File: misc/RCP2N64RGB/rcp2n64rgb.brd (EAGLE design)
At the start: 149.4 x 21.1 mm, 67 parts

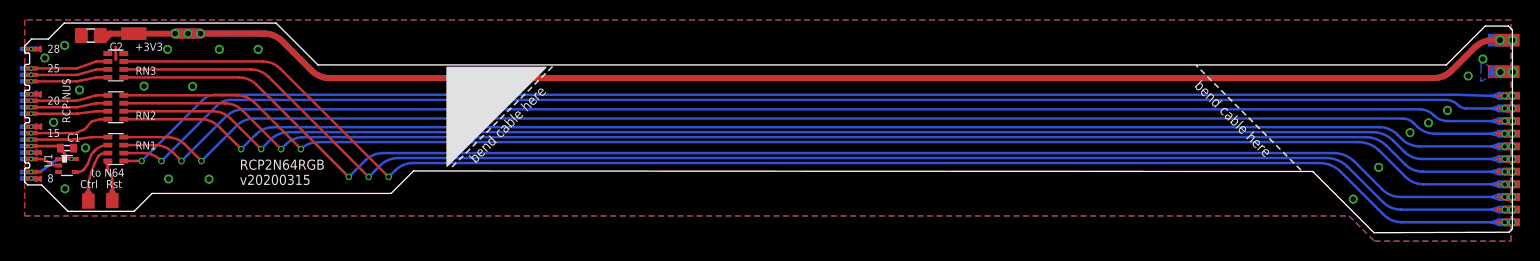
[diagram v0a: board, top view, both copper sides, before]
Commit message: update flex PCBs with suitable buffering
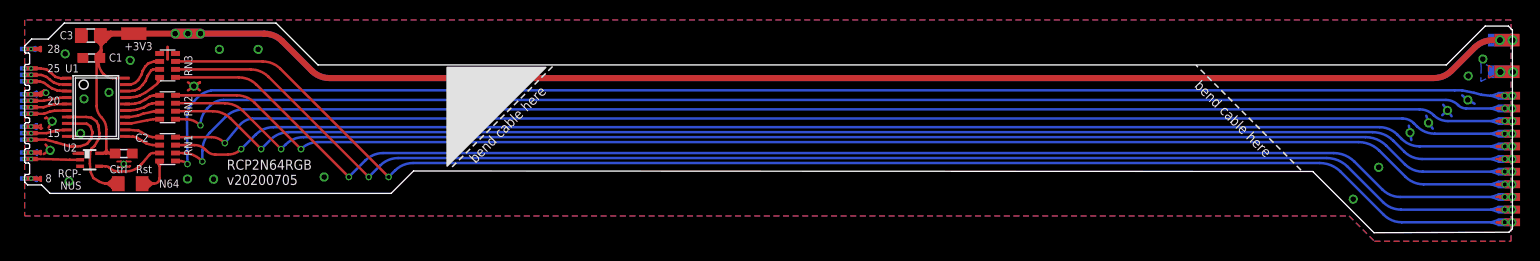
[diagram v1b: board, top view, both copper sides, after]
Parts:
- removed E$1, E$3, E$4, E$5: (no value), wirepad:SMD0,45-1,35
- added C3: 22u, rcl:C0805
- added U2: SN74LVC1G17DCKR, texas:DCK_R-PDSO-G5
- C1: value (none) -> 0.1u; device rcl:C0402 -> rcl:C0603
- C2: value 22u -> 0.1u; device rcl:C0805 -> rcl:C0603
- U1: value (none) -> 74VHC9151FT; device 74xx-little-de:DCK_R-PDSO-G5 -> sipex:TSSOP20
- moved C2 12.3 mm to (9.95, 0.55), turned to 0 degrees
- moved C1 9.38 mm to (6.70, 10.2), turned to 180 degrees
- moved U1 6.53 mm to (7.15, 5.20)
- moved RN1 5.20 mm to (14.3, 1.00)
- moved RN2 5.20 mm to (14.3, 5.20)
- moved RN3 5.20 mm to (14.3, 9.40)
- moved E$2 3.47 mm to (9.40, -2.48)
- moved E$6 3.45 mm to (11.8, -2.48)
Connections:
- removed net VCC: C1.1, E$1.P$1, E$3.P$1, E$4.P$1, E$5.P$1, U1.5
- removed net VCLK_BUF: RN1.2, U1.4
- new net S$1: RN3.2, U1.19
- new net S$10: RN2.4, U1.13
- new net S$11: RN1.3, U2.4
- new net S$12: RN1.2, U1.11
- new net S$2: RN3.3, U1.18
- new net S$3: RN3.4, U1.17
- new net S$4: RN2.1, U1.16
- new net S$6: RN2.2, U1.15
- new net S$7: RN2.3, U1.14
- new net S$9: RN1.1, U1.12
- net #DSYNC: now also U1.8; no longer RN1.1
- net 3V3: now also C1.1, C3.1, U1.20, U2.5
- net CTRL: now also U1.7; no longer RN1.3
- net CTRL.1: now also RN2.5; no longer RN1.6
- net D0: now also U1.1; no longer RN3.2
- net D1: now also U1.2; no longer RN3.3
- net D2: now also U1.3; no longer RN3.4
- net D3: now also U1.4; no longer RN2.1
- net D4: now also U1.5; no longer RN2.2
- net D5: now also U1.6; no longer RN2.3
- net D6: now also U1.9; no longer RN2.4
- net D6.1: now also RN1.7; no longer RN2.5
- net GND: now also C3.2, U1.10, U2.3; no longer U1.3
- net VCLK: now also U2.2; no longer U1.2
- net VCLK.1: now also RN1.6; no longer RN1.7
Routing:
- net 3V3: track 284.1 -> 305.7 mm
- net GND: track 18.6 -> 38.3 mm, vias 32 -> 36
- net VCC: track 10.9 -> 0.00 mm, vias 5 -> 0
- net CTRL: track 7.76 -> 14.6 mm
- net S$11: track 0.00 -> 6.83 mm
- net #DSYNC.1: track 150.5 -> 144.0 mm
- net CTRL.1: track 150.0 -> 143.7 mm
- net D6.1: track 150.1 -> 144.2 mm
- net S$3: track 0.00 -> 5.74 mm
- net D4.1: track 150.2 -> 145.0 mm
- net D5.1: track 149.7 -> 144.5 mm
- net D3.1: track 150.6 -> 145.4 mm
- net D2.1: track 153.3 -> 148.1 mm
- net D1.1: track 153.4 -> 148.2 mm
- net D0.1: track 154.2 -> 149.0 mm
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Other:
- outline, holes or cut-outs redrawn
- board text added: "N64"
- board text added: "RCP- NUS"
- board text added: "RCP2N64RGB v20200705"
- board text removed: "RCP-NUS"
- board text removed: "RCP2N64RGB v20200315"
- board text removed: "to N64"
